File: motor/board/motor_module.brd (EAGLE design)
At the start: 33.5 x 15 mm, 78 parts, among them IC6 LTC6088, IC7 DRV8833RTY

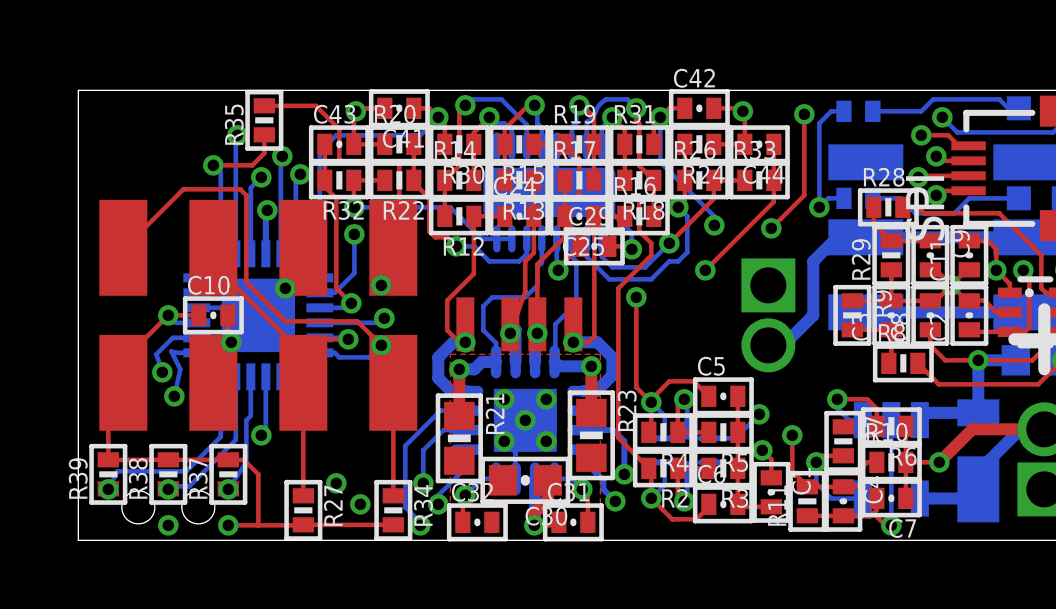
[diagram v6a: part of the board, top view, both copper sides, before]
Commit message: Full routing done. Need to do silkscreen
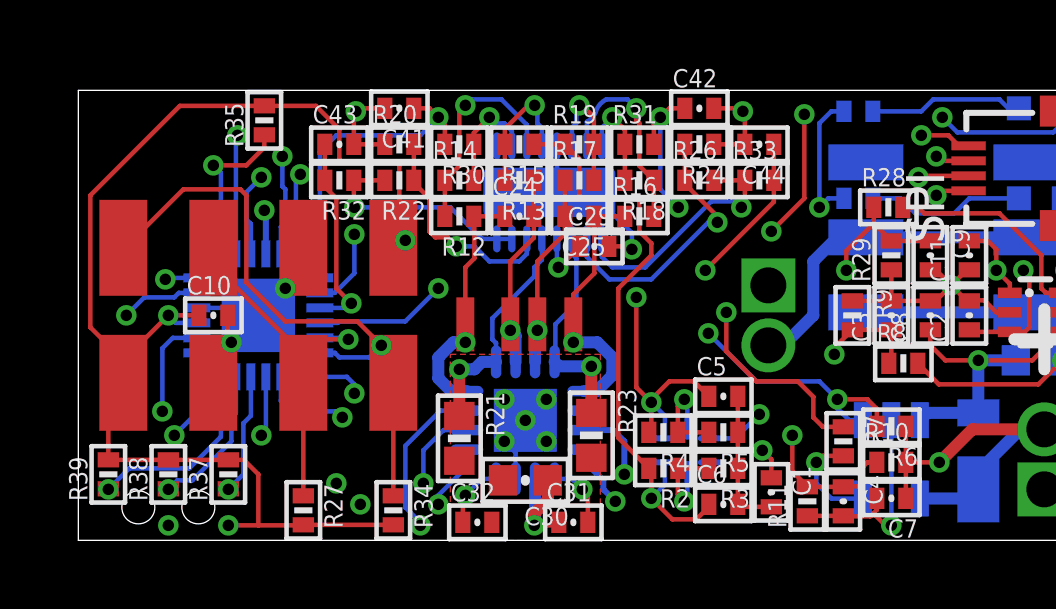
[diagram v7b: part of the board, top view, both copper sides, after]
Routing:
- net CHARGE_STATUS: track 3.34 -> 32.5 mm, vias 1 -> 3
- net CHARGE_ENABLE: track 0.00 -> 27.9 mm, vias 0 -> 2
- net SENSE_I_BATT: track 2.66 -> 29.7 mm, vias 0 -> 2
- net SENSE_V_BATT: track 2.45 -> 23.3 mm, vias 0 -> 2
- net V_3.0: track 81.8 -> 87.3 mm
- net MOTOR_B_BEMF: track 21.1 -> 19.2 mm
- net MOTOR_B_OUT2: track 7.79 -> 6.46 mm
- net N$34: track 7.08 -> 8.37 mm
- net MOTOR_A_OUT1: track 9.50 -> 8.30 mm
- net SPI_SS: track 31.4 -> 32.6 mm
- net MOTOR_B_OUT1: track 9.70 -> 8.81 mm
- net MOTOR_A_ISEN: track 8.61 -> 7.71 mm
- net SWD_DIO/STATUS: track 55.7 -> 56.3 mm
- net N$26: track 8.45 -> 9.10 mm
